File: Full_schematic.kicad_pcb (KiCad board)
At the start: 8 copper layers, 215 x 178.7 mm, 219 parts, among them IC1 XC7A100T-1FTG256C, J1 FFC3B11-40-T, J3 Conn_ST_STDC14, J5 USB_B_Micro, J6 AHDF15A-KG-TAXB, U1 2S7A_0518S1U, U10 MC14511BDG, U11 MAN72A, U12 MC14511BDG, U13 STM32U545VETxQ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

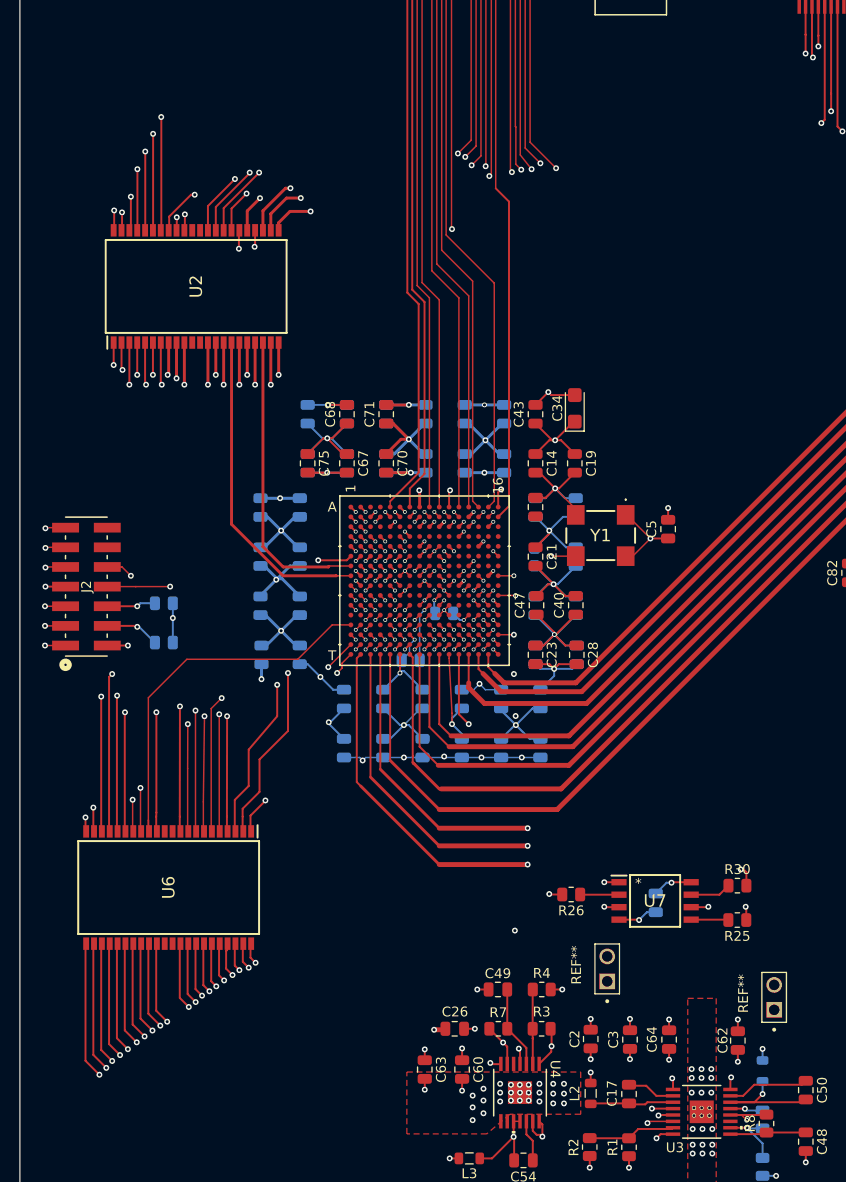
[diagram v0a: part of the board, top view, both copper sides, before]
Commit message: Added debug connector footprint++
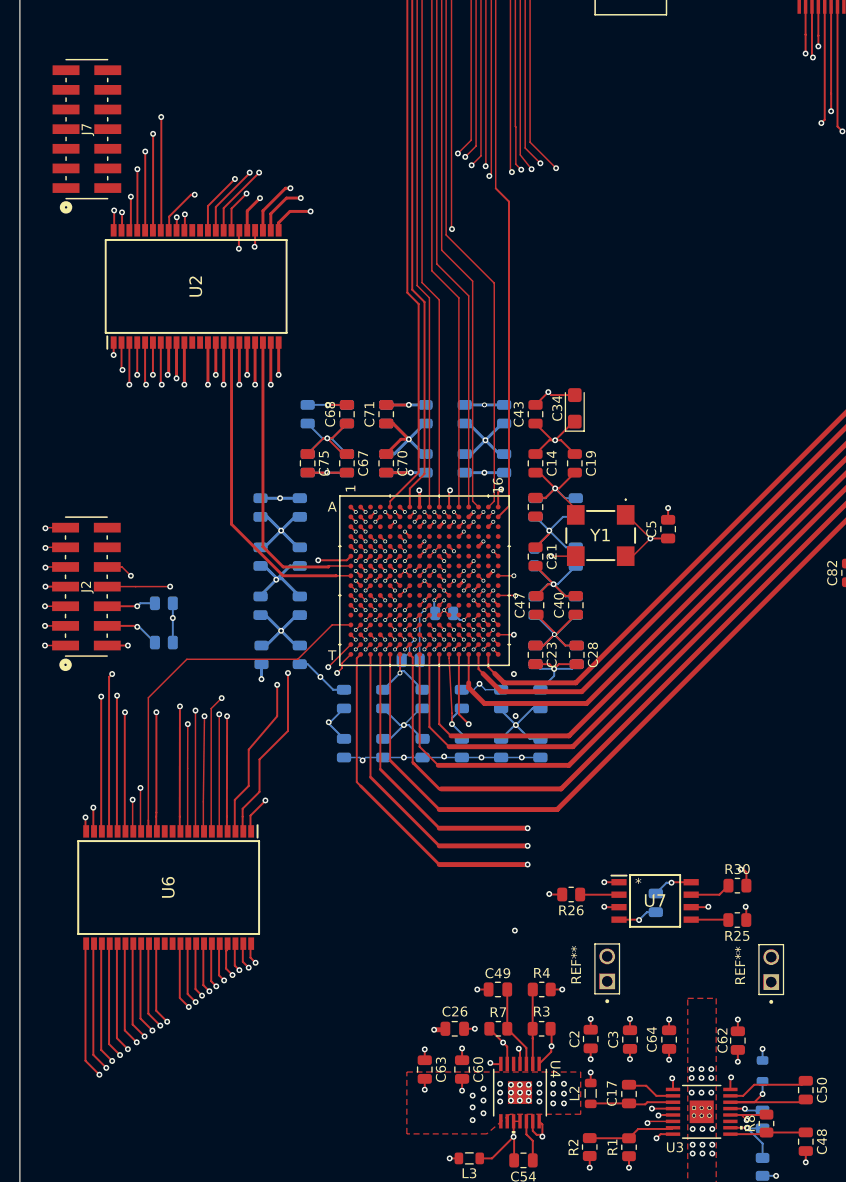
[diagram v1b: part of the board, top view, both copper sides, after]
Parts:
- added J7: ~, debug_FPGA:CONN14_877591414_MOL, F.Cu at (121.5, 107.7)
- moved REF** 2.85 mm to (191.2, 193.3)

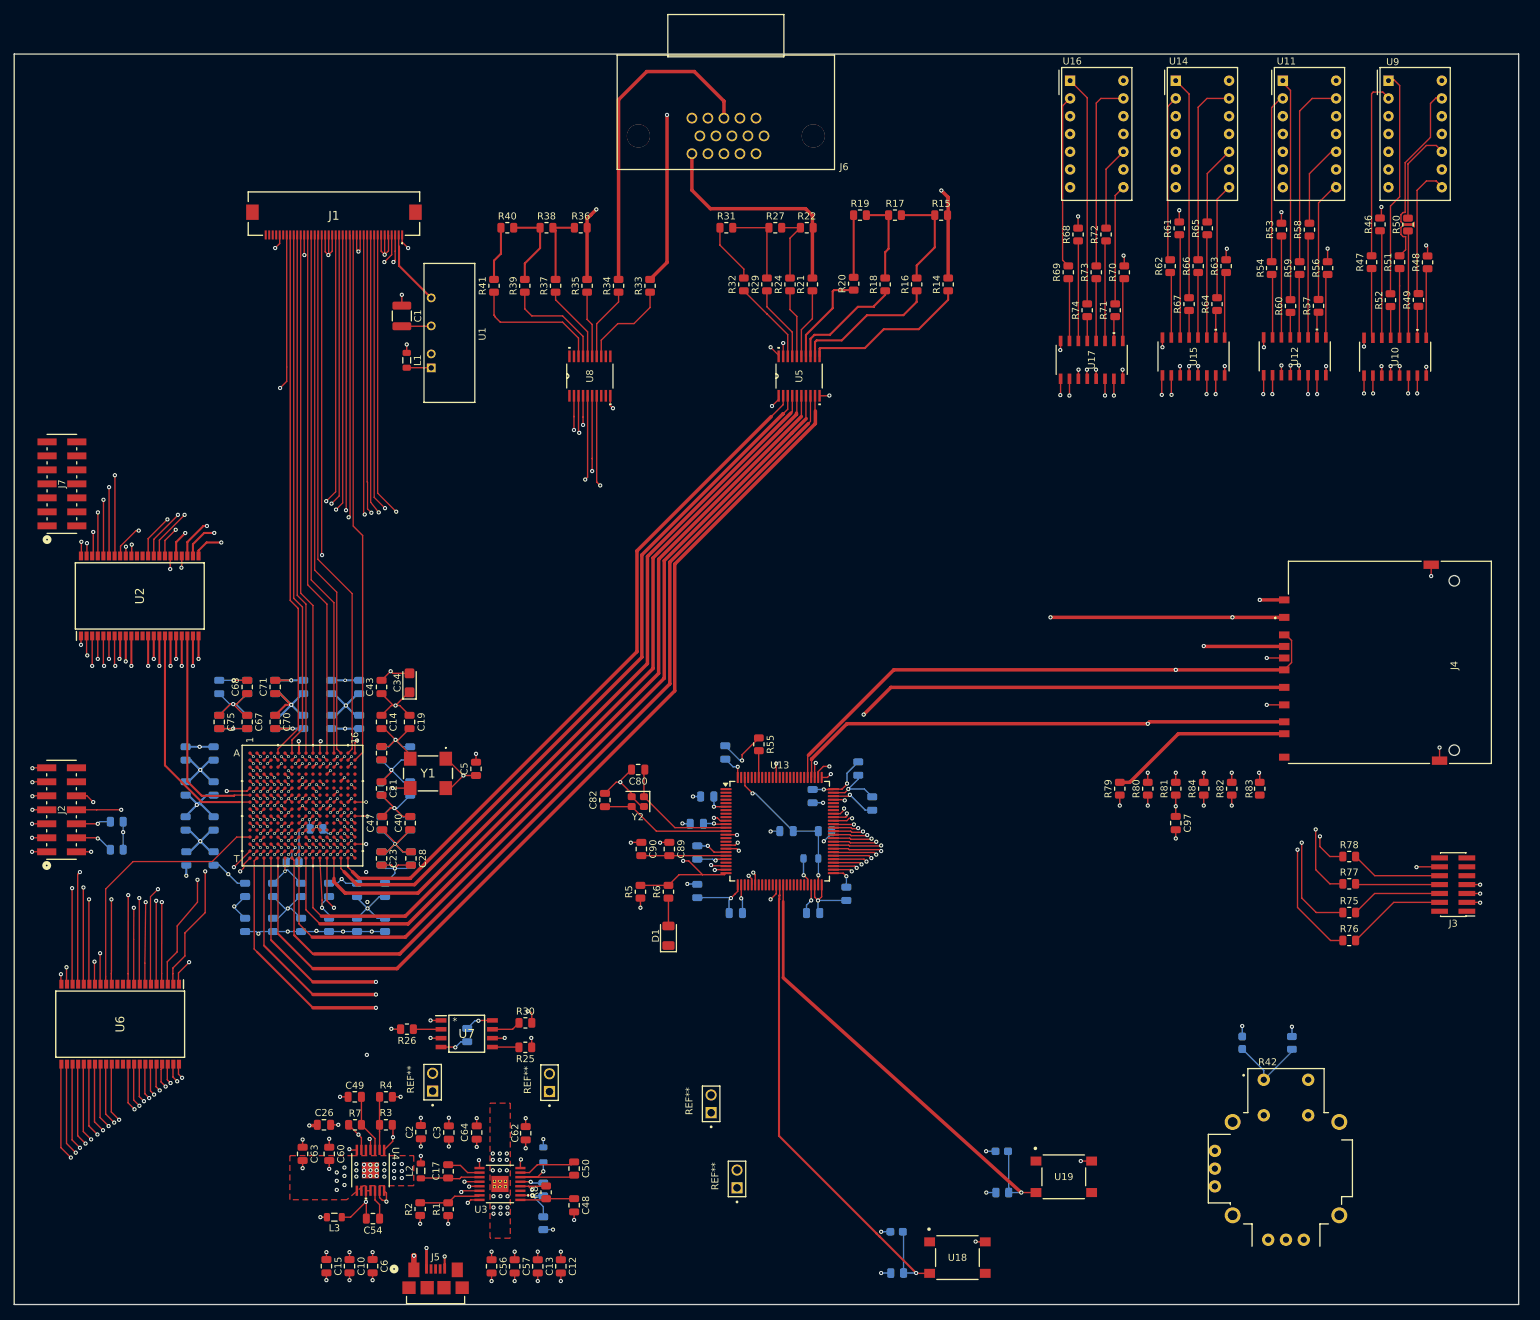
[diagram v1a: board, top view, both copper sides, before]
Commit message: Added extra pin header footprints
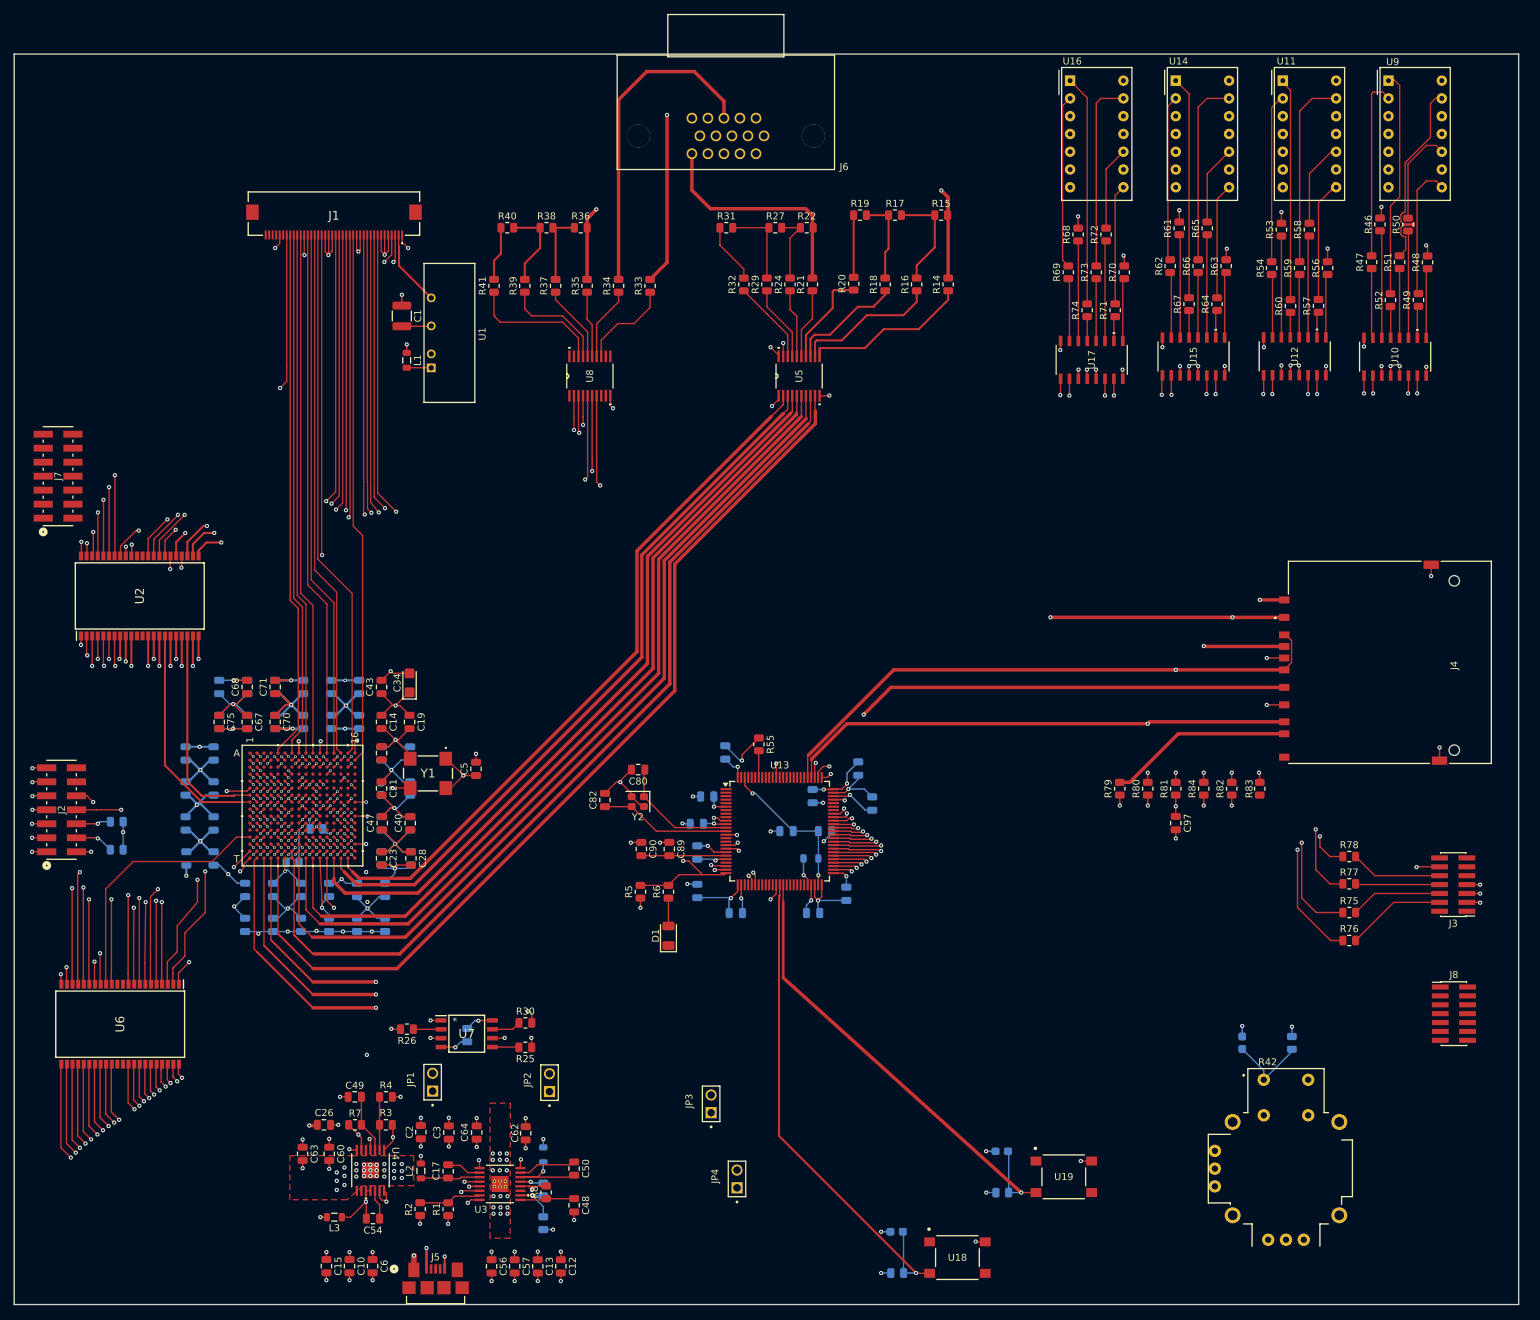
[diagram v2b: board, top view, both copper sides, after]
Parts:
- added J8: Conn_ST_STDC14, Connector_PinHeader_1.27mm:PinHeader_2x07_P1.27mm_Vertical_SMD, F.Cu at (320.4, 183.4)
- J7: value ~ -> CONN14_877591414_MOL
- moved J7 1.23 mm to (121.0, 106.6)
- renumbered REF** to JP1, REF** to JP2, REF** to JP3, REF** to JP4

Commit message: connected extra header to fpga, 4 extra connections between mcu and fpga and made pcb smaller
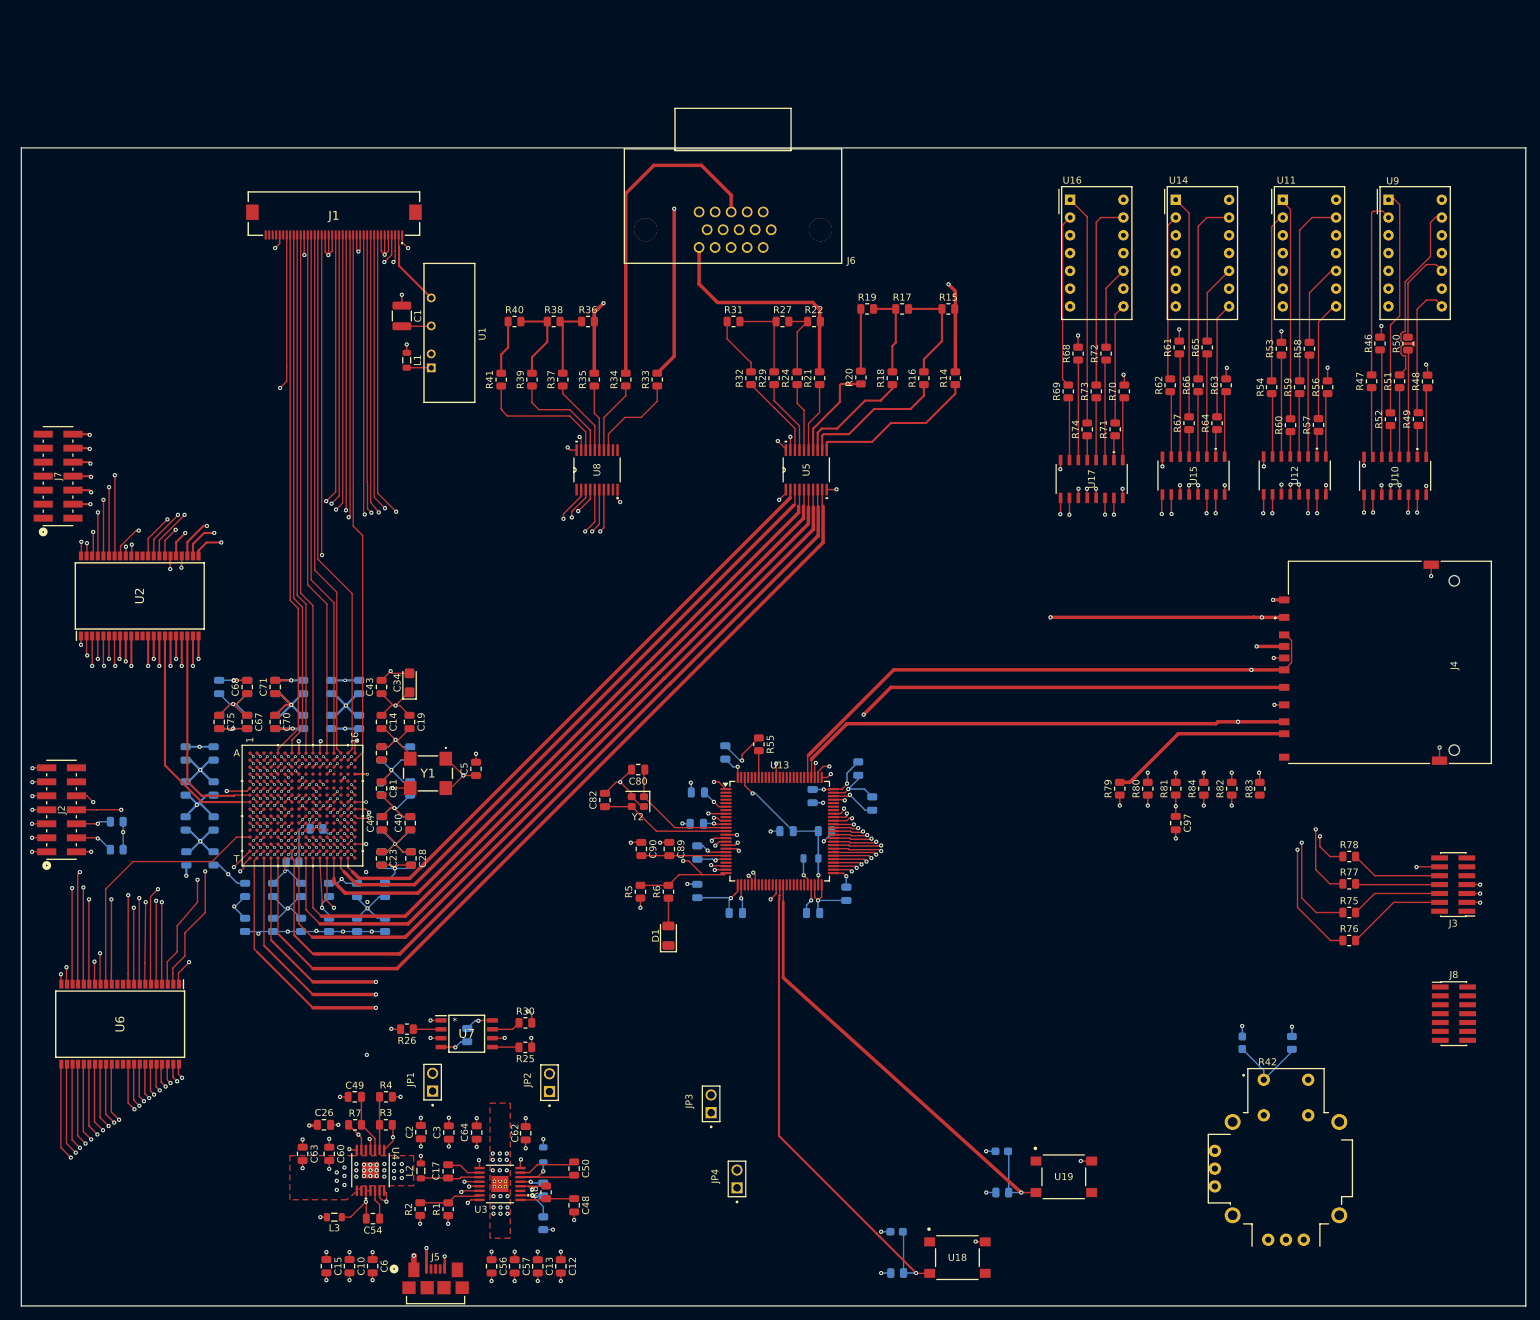
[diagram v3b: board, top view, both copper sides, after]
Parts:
- moved R46 17.0 mm to (309.9, 87.6)
- moved R68 17.0 mm to (266.7, 89.1)
- moved R72 17.0 mm to (270.7, 89.1)
- moved U10 17.0 mm to (312.0, 106.5)
- moved U12 17.0 mm to (297.7, 106.5)
- moved R47 17.0 mm to (308.7, 93.0)
- moved R48 17.0 mm to (316.7, 93.1)
- moved R49 17.0 mm to (315.4, 98.4)
- moved R50 17.0 mm to (313.9, 87.7)
- moved R51 17.0 mm to (312.7, 93.0)
- moved R52 17.0 mm to (311.4, 98.5)
- moved R53 17.0 mm to (295.8, 88.4)
- moved R54 17.0 mm to (294.4, 93.9)
- moved R56 17.0 mm to (302.4, 93.9)
- moved R57 17.0 mm to (301.1, 99.3)
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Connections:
- IC1 pad C6: unconnected-(IC1-IO_L5N_T0_AD13N_35-PadC6) -> C6
- IC1 pad C7: unconnected-(IC1-IO_L5P_T0_AD13P_35-PadC7) -> C7
- IC1 pad D16: unconnected-(IC1-IO_L17N_T2_A25_15-PadD16) -> D16
- IC1 pad D5: unconnected-(IC1-IO_L6N_T0_VREF_35-PadD5) -> D5
- IC1 pad D8: unconnected-(IC1-IO_L6P_T0_15-PadD8) -> D8
- IC1 pad G16: unconnected-(IC1-IO_L22N_T3_A16_15-PadG16) -> G16
- IC1 pad J15: unconnected-(IC1-IO_L23P_T3_FOE_B_15-PadJ15) -> J15
- IC1 pad J16: unconnected-(IC1-IO_L23N_T3_FWE_B_15-PadJ16) -> J16
- J7 pad 10: (no net) -> C6
- J7 pad 12: (no net) -> C7
- J7 pad 14: (no net) -> D8
- J7 pad 4: (no net) -> C3
- J7 pad 6: (no net) -> C4
- J7 pad 8: (no net) -> D5
- U13 pad 1: unconnected-(U13-PE2-Pad1) -> D16
- U13 pad 15: unconnected-(U13-PC0-Pad15) -> J15
- U13 pad 16: unconnected-(U13-PC1-Pad16) -> J16
- U13 pad 8: unconnected-(U13-PC14-Pad8) -> G16
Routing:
- net D8: track 0.00 -> 69.7 mm, vias 0 -> 2
- net C7: track 0.00 -> 67.4 mm, vias 0 -> 2
- net C6: track 0.00 -> 65.9 mm, vias 0 -> 2
- net D5: track 0.00 -> 64.2 mm, vias 0 -> 2
- net C4: track 0.00 -> 61.6 mm, vias 0 -> 2
- net C3: track 0.00 -> 60.9 mm, vias 0 -> 2
- net J15: track 0.00 -> 57.8 mm, vias 0 -> 2
- net G16: track 0.00 -> 56.5 mm, vias 0 -> 2
- net J16: track 0.00 -> 55.5 mm, vias 0 -> 2
- net D16: track 0.00 -> 55.2 mm, vias 0 -> 2
- net PA9: track 76.2 -> 59.2 mm
- net PD15: track 88.7 -> 71.7 mm
- net PC7: track 83.0 -> 66.0 mm
- net PC6: track 87.2 -> 70.2 mm
- net PA8: track 77.7 -> 60.6 mm
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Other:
- board size 215 x 178.7 mm -> 215 x 165.5 mm

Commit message: Added logo
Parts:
- moved JP3 47.0 mm to (167.8, 189.6)
- moved JP4 43.4 mm to (191.4, 172.8)
- moved J8 8.31 mm to (320.1, 175.1)
- moved R75 6.96 mm to (305.7, 162.0)
- moved R76 6.96 mm to (305.7, 166.0)
- moved R78 6.96 mm to (305.7, 154.0)
- moved R77 6.86 mm to (305.7, 158.0)
- moved J3 5.96 mm to (320.1, 159.0)
- moved R26 1.69 mm to (171.3, 184.0)
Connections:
- J1 pad 4: +3.3V -> +3V3
- J8 pad 1: (no net) -> PB11
- J8 pad 11: (no net) -> PE12
- J8 pad 3: (no net) -> PB10
- J8 pad 5: (no net) -> PE15
- J8 pad 7: (no net) -> PE14
- J8 pad 9: (no net) -> PE13
- JP3 pad 1: (no net) -> +1V0
- JP3 pad 2: (no net) -> +1V0
- JP4 pad 1: (no net) -> Net-(J5-VBUS)
- JP4 pad 2: (no net) -> Net-(J5-VBUS)
- U13 pad 40: unconnected-(U13-PE12-Pad40) -> PE12
- U13 pad 41: unconnected-(U13-PE13-Pad41) -> PE13
- U13 pad 42: unconnected-(U13-PE14-Pad42) -> PE14
- U13 pad 43: unconnected-(U13-PE15-Pad43) -> PE15
- U13 pad 44: unconnected-(U13-PB10-Pad44) -> PB10
- U13 pad 45: unconnected-(U13-PB11-Pad45) -> PB11
- U5 pad 20: +3.3V -> +3V3
- U8 pad 20: +3.3V -> +3V3
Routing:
- net PE12: track 0.00 -> 99.6 mm, vias 0 -> 2
- net PE13: track 0.00 -> 98.6 mm, vias 0 -> 2
- net PE14: track 0.00 -> 97.5 mm, vias 0 -> 2
- net PE15: track 0.00 -> 96.5 mm, vias 0 -> 2
- net PB10: track 0.00 -> 95.4 mm, vias 0 -> 2
- net PB11: track 0.00 -> 94.3 mm, vias 0 -> 2
- net +3.3V: track 58.0 -> 50.5 mm, vias 18 -> 15
- net +3V3: track 181.3 -> 188.7 mm, vias 56 -> 59
- net Net-(U13-PA14): track 87.5 -> 80.2 mm
- net Net-(U13-PA13): track 86.0 -> 79.0 mm
- net Net-(U13-PB3): track 94.2 -> 88.4 mm
- net +1V0: track 124.9 -> 122.4 mm
- net Net-(J3-~{RST}): track 105.6 -> 107.8 mm
- net Net-(U13-PA15): track 82.3 -> 83.7 mm
- net Net-(J5-VBUS): track 164.9 -> 163.7 mm
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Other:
- board size 215 x 165.5 mm -> 212 x 165.5 mm
- board text added: "H2025"
- board text added: "Mads Engesvoll Jørgen Fjermedal Paulius Juzenas Jørgen Nikolaisen"
- board text added: "Rikke Schjønsby Nicolai Sommervold David Salguero Spilde"
